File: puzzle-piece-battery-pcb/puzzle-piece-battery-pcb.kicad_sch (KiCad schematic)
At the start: 18 parts, among them J1 Lipo, J2 INPUT, J3 OUTPUT, J4 GND Rivet, J5 5V Rivet, J6 3.3V Rivet, U2 MCP73831T-2ACI/OT, U3 LM3480-3.3

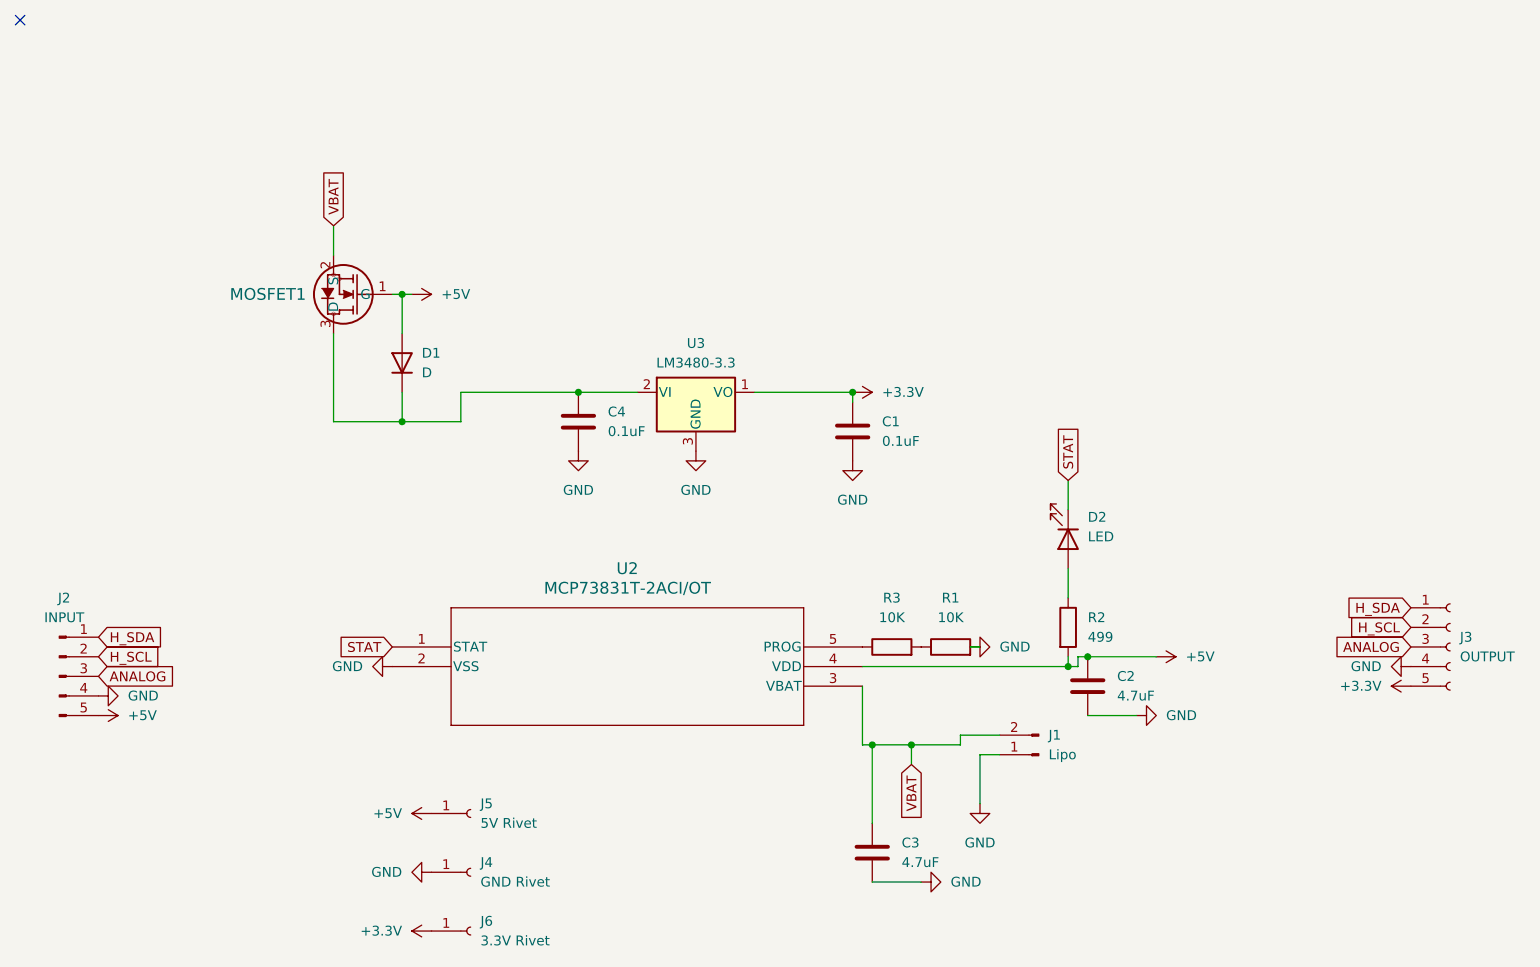
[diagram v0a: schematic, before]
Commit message: made battery controller singled sided and removed lipo
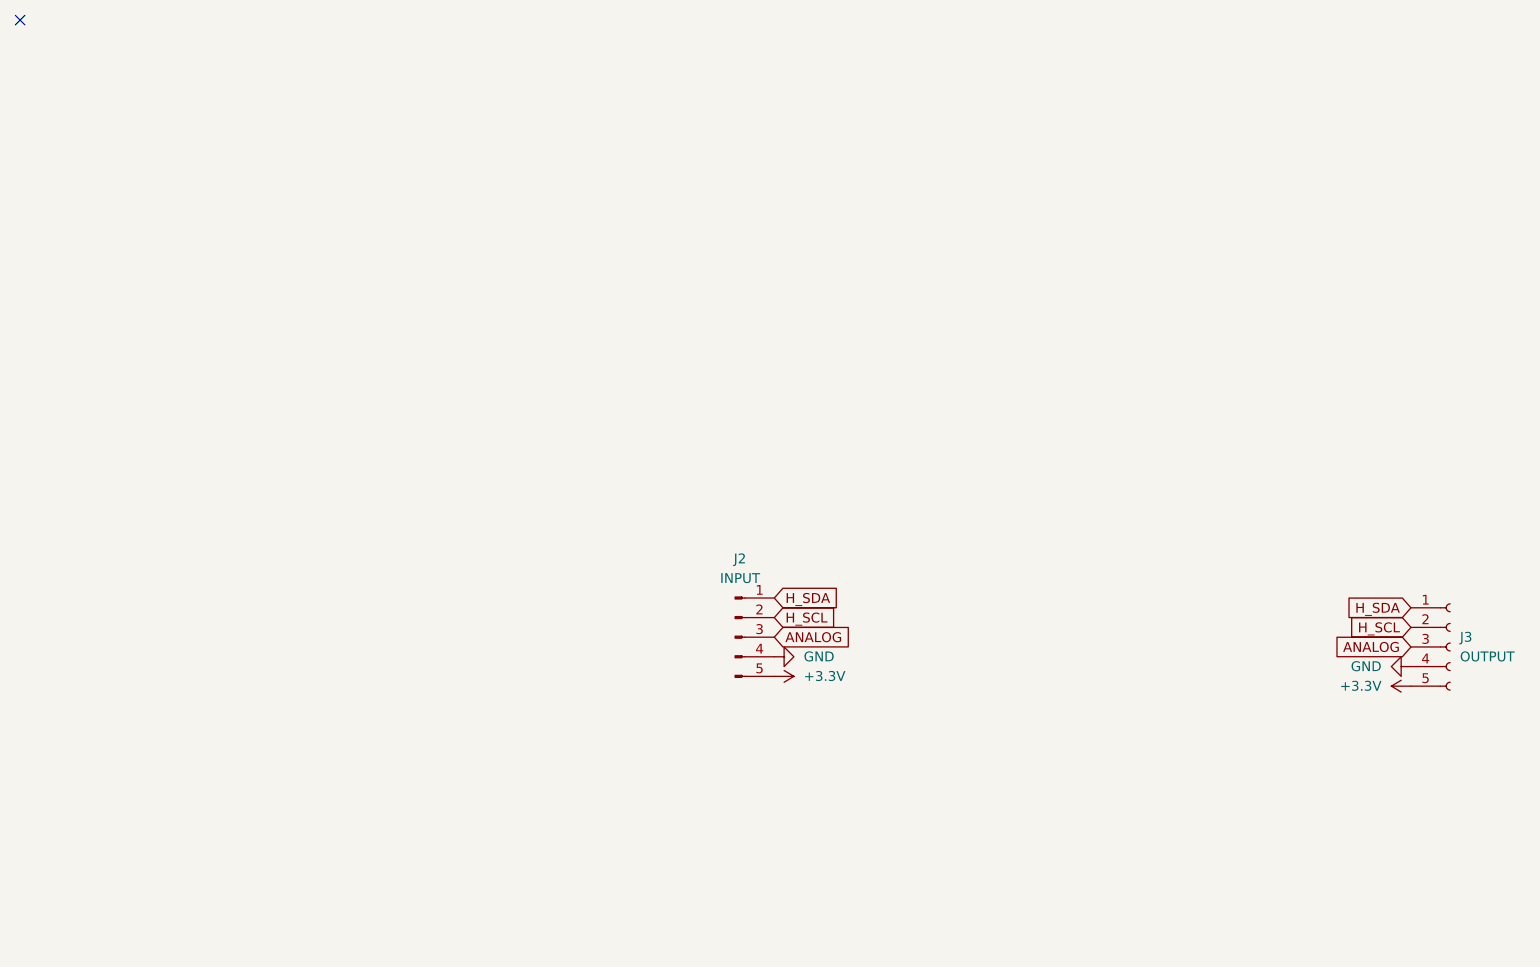
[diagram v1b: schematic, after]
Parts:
- removed C1, C4: 0.1uF, Capacitor_SMD:C_1206_3216Metric_Pad1.33x1.80mm_HandSolder, symbol Device:C
- removed C2, C3: 4.7uF, Capacitor_THT:C_Disc_D5.0mm_W2.5mm_P2.50mm, symbol Device:C
- removed D1: D, Diode_SMD:D_1206_3216Metric_Pad1.42x1.75mm_HandSolder, symbol Device:D
- removed D2: LED, LED_SMD:LED_1206_3216Metric_Pad1.42x1.75mm_HandSolder, symbol Device:LED
- removed J1: Lipo, Connector_PinSocket_2.54mm:PinSocket_1x02_P2.54mm_Vertical, symbol Connector:Conn_01x02_Pin
- removed J4: GND Rivet, Connector_PinSocket_2.54mm:PinSocket_1x01_P2.54mm_Vertical, symbol Connector:Conn_01x01_Socket
- removed J5: 5V Rivet, Connector_PinSocket_2.54mm:PinSocket_1x01_P2.54mm_Vertical, symbol Connector:Conn_01x01_Socket
- removed J6: 3.3V Rivet, Connector_PinSocket_2.54mm:PinSocket_1x01_P2.54mm_Vertical, symbol Connector:Conn_01x01_Socket
- removed MOSFET1: ZXM61P03FTA, ZXM61P03FTA:SOT23_ZETEX_DIO, symbol ZXM61P03FTA:ZXM61P03FTA
- removed R1, R3: 10K, Resistor_SMD:R_1206_3216Metric_Pad1.30x1.75mm_HandSolder, symbol Device:R
- removed R2: 499, Resistor_SMD:R_1206_3216Metric_Pad1.30x1.75mm_HandSolder, symbol Device:R
- removed U2: MCP73831T-2ACI/OT, MCP73831T_2ACI_OT:SOT-23-5_MC_MCH, symbol MCP73831T_2ACI_OT:MCP73831T-2ACI_OT
- removed U3: LM3480-3.3, Package_TO_SOT_SMD:SOT-23, symbol Regulator_Linear:LM3480-3.3
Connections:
- net +5V is gone; now on net +3.3V: J2.5 (Pin_5)
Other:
- moved on the sheet: J2

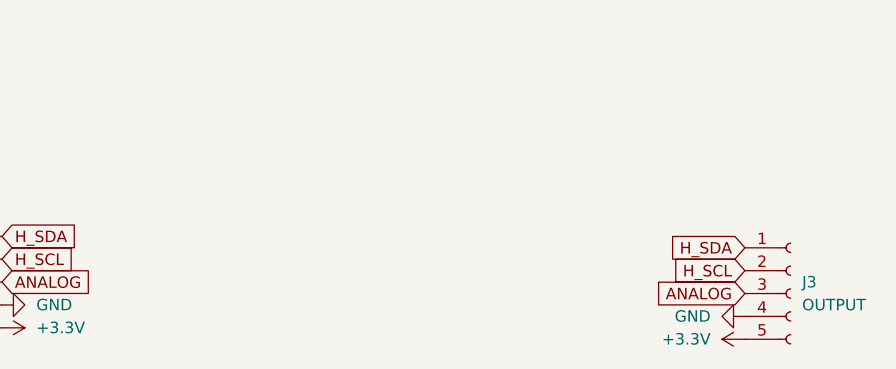
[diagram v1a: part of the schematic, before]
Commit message: add unrouted output throughholes to controller, and mounting holes
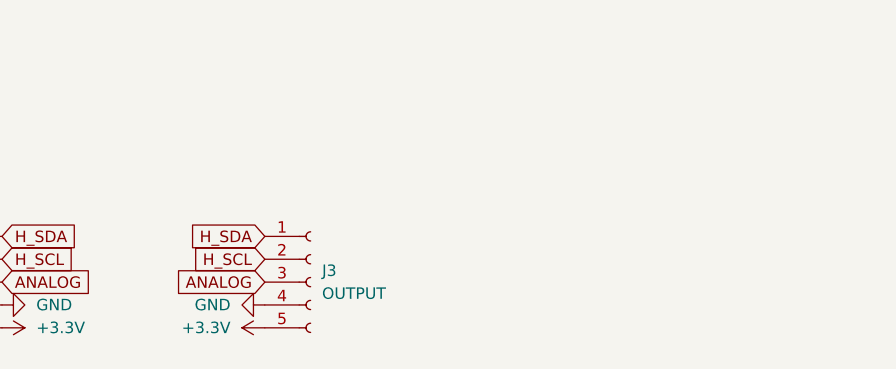
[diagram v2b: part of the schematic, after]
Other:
- moved on the sheet: J3
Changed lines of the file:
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@@
 	(global_label "ANALOG"
 		(shape input)
-		(at 232.41 111.76 180)
+		(at 179.07 110.49 180)
 		(fields_autoplaced yes)
 		(effects
@@
 		)
 		(property "Intersheetrefs" "${INTERSHEET_REFS}"
-			(at 222.2885 111.76 0)
+			(at 168.9485 110.49 0)
 			(effects
 				(font
@@
 	(global_label "H_SCL"
 		(shape input)
-		(at 232.41 109.22 180)
+		(at 179.07 107.95 180)
 		(fields_autoplaced yes)
 		(effects
@@
 		)
 		(property "Intersheetrefs" "${INTERSHEET_REFS}"
-			(at 223.6191 109.22 0)
+			(at 170.2791 107.95 0)
 			(effects
 				(font
@@
 	(global_label "H_SDA"
 		(shape input)
-		(at 232.41 106.68 180)
+		(at 179.07 105.41 180)
 		(fields_autoplaced yes)
 		(effects
@@
 		)
 		(property "Intersheetrefs" "${INTERSHEET_REFS}"
-			(at 223.5586 106.68 0)
+			(at 170.2186 105.41 0)
 			(effects
 				(font
@@
 	(symbol
 		(lib_id "power:+3.3V")
-		(at 232.41 116.84 90)
+		(at 179.07 115.57 90)
 		(unit 1)
 		(exclude_from_sim no)
@@
 		(fields_autoplaced yes)
 		(property "Reference" "#PWR012"
-			(at 236.22 116.84 0)
+			(at 182.88 115.57 0)
 			(effects
 				(font
@@
 		)
 		(property "Value" "+3.3V"
-			(at 228.6 116.8399 90)
+			(at 175.26 115.5699 90)
 			(effects
 				(font
@@
 		)
 		(property "Footprint" ""
-			(at 232.41 116.84 0)
+			(at 179.07 115.57 0)
 			(effects
 				(font
@@
 		)
 		(property "Datasheet" ""
-			(at 232.41 116.84 0)
+			(at 179.07 115.57 0)
 			(effects
 				(font
@@
 		)
 		(property "Description" "Power symbol creates a global label with name \"+3.3V\""
-			(at 232.41 116.84 0)
+			(at 179.07 115.57 0)
 			(effects
 				(font
@@
 	(symbol
 		(lib_id "power:GND")
-		(at 232.41 114.3 270)
+		(at 179.07 113.03 270)
 		(unit 1)
 		(exclude_from_sim no)
@@
 		(fields_autoplaced yes)
 		(property "Reference" "#PWR03"
-			(at 226.06 114.3 0)
+			(at 172.72 113.03 0)
 			(effects
 				(font
@@
 		)
 		(property "Value" "GND"
-			(at 228.6 114.2999 90)
+			(at 175.26 113.0299 90)
 			(effects
 				(font
@@
 		)
 		(property "Footprint" ""
-			(at 232.41 114.3 0)
+			(at 179.07 113.03 0)
 			(effects
 				(font
@@
 		)
 		(property "Datasheet" ""
-			(at 232.41 114.3 0)
+			(at 179.07 113.03 0)
 			(effects
 				(font
@@
 		)
 		(property "Description" "Power symbol creates a global label with name \"GND\" , ground"
-			(at 232.41 114.3 0)
+			(at 179.07 113.03 0)
 			(effects
 				(font
@@
 	(symbol
 		(lib_id "Connector:Conn_01x05_Socket")
-		(at 237.49 111.76 0)
+		(at 184.15 110.49 0)
 		(unit 1)
 		(exclude_from_sim no)
@@
 		(fields_autoplaced yes)
 		(property "Reference" "J3"
-			(at 238.76 110.4899 0)
+			(at 185.42 109.2199 0)
 			(effects
 				(font
@@
 		)
 		(property "Value" "OUTPUT"
-			(at 238.76 113.0299 0)
+			(at 185.42 111.7599 0)
 			(effects
 				(font
@@
 		)
 		(property "Footprint" "Connector_PinSocket_2.54mm:PinSocket_1x05_P2.54mm_Vertical"
-			(at 237.49 111.76 0)
+			(at 184.15 110.49 0)
 			(effects
 				(font
@@
 		)
 		(property "Datasheet" "~"
-			(at 237.49 111.76 0)
+			(at 184.15 110.49 0)
 			(effects
 				(font
@@
 		)
 		(property "Description" "Generic connector, single row, 01x05, script generated"
-			(at 237.49 111.76 0)
-			(effects
-				(font
+			(at 184.15 110.49 0)
+			(effects
+				(font
